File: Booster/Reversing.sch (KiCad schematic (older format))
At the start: 13 parts

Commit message: Getting close to feature complete for a single channel.
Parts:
- removed R?: R, symbol R
- added P?: REVERSER_OUT_OP, symbol CONN_01X02
- added R?: R, symbol R
- added U?: PC817, Housings_DIP:DIP-4_W7.62mm, symbol PC817
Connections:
- wire segments 33 -> 49
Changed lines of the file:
@@
 	0    1    1    0
 $EndComp
-Wire Wire Line
-	3050 4400 4250 4400
-Wire Wire Line
-	4250 4600 3050 4600
 $Comp
 L +5V #PWR?
@@
 	-1   0    0    1
 $EndComp
-Wire Wire Line
-	2750 4400 2600 4400
-Wire Wire Line
-	2600 4400 2600 4950
-Wire Wire Line
-	2750 4600 2600 4600
-Connection ~ 2600 4600
 Text Label 3500 4600 0    60   ~ 0
 IR_Led
@@
 	1    0    0    -1
 $EndComp
-Wire Wire Line
-	4100 4100 4100 4200
-Wire Wire Line
-	4100 4200 4250 4200
 $Comp
 L LM339 U?
@@
 	1    0    0    -1
 $EndComp
-Wire Wire Line
-	4050 3450 4800 3450
-Wire Wire Line
-	4300 3450 4300 3300
-Wire Wire Line
-	4600 3450 4600 2700
-Wire Wire Line
-	4600 2700 4850 2700
-Connection ~ 4300 3450
 $Comp
 L +5V #PWR?
@@
 	1    0    0    -1
 $EndComp
-Wire Wire Line
-	4300 2900 4300 3000
-Wire Wire Line
-	3150 4400 3150 3550
-Wire Wire Line
-	3150 3550 3450 3550
-Connection ~ 3150 4400
 $Comp
 L POT_TRIM RV?
@@
 	1    0    0    -1
 $EndComp
-Wire Wire Line
-	2950 3350 3450 3350
-Wire Wire Line
-	2800 3500 2800 3700
-Wire Wire Line
-	2800 2900 2800 3200
 $Comp
 L +5V #PWR?
@@
 	1    0    0    -1
 $EndComp
-Wire Wire Line
-	2350 2500 4850 2500
-Wire Wire Line
-	7250 2600 6050 2600
 $Comp
 L BC807-40 Q?
@@
 	0    1    1    0
 $EndComp
-Connection ~ 4600 3450
-Wire Wire Line
-	5100 3450 5300 3450
 $Comp
 L LED D?
@@
 	0    1    1    0
 $EndComp
-Wire Wire Line
-	5600 3250 5600 3150
-Wire Wire Line
-	5600 3150 6450 3150
-Wire Wire Line
-	6750 3150 7000 3150
-Wire Wire Line
-	7300 3150 7400 3150
-Wire Wire Line
-	7400 3150 7400 3800
-Wire Wire Line
-	5600 3650 5600 4050
-Wire Wire Line
-	5600 4050 5350 4050
-Wire Wire Line
-	5350 4050 5350 3900
 $Comp
 L +5V #PWR?
@@
 $EndComp
 Wire Wire Line
+	3050 4400 3150 4400
+Wire Wire Line
+	3150 4400 4250 4400
+Wire Wire Line
+	4250 4600 3050 4600
+Wire Wire Line
+	2750 4400 2600 4400
+Wire Wire Line
+	2600 4400 2600 4600
+Wire Wire Line
+	2600 4600 2600 4950
+Wire Wire Line
+	2750 4600 2600 4600
+Connection ~ 2600 4600
+Wire Wire Line
+	4100 4100 4100 4200
+Wire Wire Line
+	4100 4200 4250 4200
+Wire Wire Line
+	4050 3450 4300 3450
+Wire Wire Line
+	4300 3450 4600 3450
+Wire Wire Line
+	4600 3450 4800 3450
+Wire Wire Line
+	4300 3450 4300 3300
+Wire Wire Line
+	4600 2700 4600 3450
+Wire Wire Line
+	4600 3450 4600 3800
+Wire Wire Line
+	4600 2700 4850 2700
+Connection ~ 4300 3450
+Wire Wire Line
+	4300 2900 4300 3000
+Wire Wire Line
+	3150 4400 3150 3550
+Wire Wire Line
+	3150 3550 3450 3550
+Connection ~ 3150 4400
+Wire Wire Line
+	2950 3350 3450 3350
+Wire Wire Line
+	2800 3500 2800 3700
+Wire Wire Line
+	2800 2900 2800 3200
+Wire Wire Line
+	2350 2500 4850 2500
+Wire Wire Line
+	7250 2600 6050 2600
+Connection ~ 4600 3450
+Wire Wire Line
+	5100 3450 5300 3450
+Wire Wire Line
+	5600 3250 5600 3150
+Wire Wire Line
+	5600 3150 6350 3150
+Wire Wire Line
+	6350 3150 6450 3150
+Wire Wire Line
+	6750 3150 7000 3150
+Wire Wire Line
+	7300 3150 7400 3150
+Wire Wire Line
+	7400 3150 7400 3800
+Wire Wire Line
+	5600 3650 5600 4050
+Wire Wire Line
+	5600 4050 5350 4050
+Wire Wire Line
+	5350 4050 5350 3900
+Wire Wire Line
 	6350 3150 6350 3750
+Wire Wire Line
+	6350 3750 6350 4400
 Wire Wire Line
 	6350 3750 6500 3750
 Connection ~ 6350 3150
+Wire Wire Line
+	6500 3850 6450 3850
+Wire Wire Line
+	6450 3850 6450 4100
+$Comp
+L GND #PWR?
+U 1 1 5A0EF583
+P 6450 4100
+F 0 "#PWR?" H 6450 3850 50  0001 C CNN
+F 1 "GND" H 6450 3950 50  0000 C CNN
+F 2 "" H 6450 4100 50  0001 C CNN
+F 3 "" H 6450 4100 50  0001 C CNN
+	1    6450 4100
+	1    0    0    -1
+$EndComp
+Connection ~ 6350 3750
 $Comp
 L R R?
-U 1 1 5A08AD53
-P 6200 3500
-F 0 "R?" V 6280 3500 50  0000 C CNN
-F 1 "R" V 6200 3500 50  0000 C CNN
-F 2 "" V 6130 3500 50  0000 C CNN
-F 3 "" H 6200 3500 50  0000 C CNN
-	1    6200 3500
-	1    0    0    -1
-$EndComp
-Wire Wire Line
-	6200 3350 6200 3150
-Connection ~ 6200 3150
-Wire Wire Line
-	6200 3650 6200 4100
-Wire Wire Line
-	6500 3850 6200 3850
-Connection ~ 6200 3850
-$Comp
-L GND #PWR?
-U 1 1 5A08AE8D
-P 6200 4100
-F 0 "#PWR?" H 6200 3850 50  0001 C CNN
-F 1 "GND" H 6200 3950 50  0000 C CNN
-F 2 "" H 6200 4100 50  0000 C CNN
-F 3 "" H 6200 4100 50  0000 C CNN
-	1    6200 4100
-	1    0    0    -1
-$EndComp
+U 1 1 5A0EF5E4
+P 6350 4550
+F 0 "R?" V 6430 4550 50  0000 C CNN
+F 1 "R" V 6350 4550 50  0000 C CNN
+F 2 "" V 6280 4550 50  0001 C CNN
+F 3 "" H 6350 4550 50  0001 C CNN
+	1    6350 4550
+	1    0    0    -1
+$EndComp
+Wire Wire Line
+	6350 4700 6350 4800
+Wire Wire Line
+	6350 4800 6550 4800
+$Comp
+L PC817 U?
+U 1 1 5A0EF66A
+P 6850 4900
+F 0 "U?" H 6650 5100 50  0000 L CNN
+F 1 "PC817" H 6850 5100 50  0000 L CNN
+F 2 "Housings_DIP:DIP-4_W7.62mm" H 6650 4700 50  0001 L CIN
+F 3 "" H 6850 4900 50  0001 L CNN
+	1    6850 4900
+	1    0    0    -1
+$EndComp
+$Comp
+L CONN_01X02 P?
+U 1 1 5A0EF6BB
+P 7650 4900
+F 0 "P?" H 7650 5050 50  0000 C CNN
+F 1 "REVERSER_OUT_OP" V 7750 4900 50  0000 C CNN
+F 2 "" H 7650 4900 50  0000 C CNN
+F 3 "" H 7650 4900 50  0000 C CNN
+	1    7650 4900
+	1    0    0    -1
+$EndComp
+Wire Wire Line
+	7450 4850 7350 4850
+Wire Wire Line
+	7350 4850 7350 4800
+Wire Wire Line
+	7350 4800 7150 4800
+Wire Wire Line
+	7150 5000 7350 5000
+Wire Wire Line
+	7350 5000 7350 4950
+Wire Wire Line
+	7350 4950 7450 4950
+$Comp
+L GND #PWR?
+U 1 1 5A0EF7FA
+P 6350 5200
+F 0 "#PWR?" H 6350 4950 50  0001 C CNN
+F 1 "GND" H 6350 5050 50  0000 C CNN
+F 2 "" H 6350 5200 50  0001 C CNN
+F 3 "" H 6350 5200 50  0001 C CNN
+	1    6350 5200
+	1    0    0    -1
+$EndComp
+Wire Wire Line
+	6350 5200 6350 5000
+Wire Wire Line
+	6350 5000 6550 5000
 $EndSCHEMATC

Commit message: Added meassurement tabs and other general "finalizing touches"
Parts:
- removed J?: Screw_Terminal_1x03, symbol Screw_Terminal_1x03
- added J? (x2): Conn_01x01, symbol Conn_01x01
- added J?: Conn_01x04, symbol Conn_01x04
- added R?: 10K, symbol R
- added R?: ?100, symbol R
- added SW?: SW_SPST_x02, symbol SW_SPST_x02
- added U?: 74HC86, symbol 74LS86
- R?: value 100 -> 220
- R?: value R -> 10K
- U?: value 74LS86 -> 74HC86
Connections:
- net labels added: Indicator_LED
- wire segments 49 -> 59
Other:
- note added: "Invert detector\nFor IR reflective/direct support."
- moved on the sheet: R?, RV?, U?A

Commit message: Reference voltage of reverser is now the 1V after the resistor dropper. This allows running one wire less to the sensor unit, at the cost of the photo resistor only working off 1V.
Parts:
- removed SW?: SW_SPST_x02, symbol SW_SPST_x02
- added SW?: SW_SPST_x03, symbol SW_SPST_x03
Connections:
- wire segments 59 -> 63
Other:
- moved on the sheet: R?
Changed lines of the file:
@@
 L R R?
 U 1 1 5A089B6E
-P 1250 4300
-F 0 "R?" V 1330 4300 50  0000 C CNN
-F 1 "10K" V 1250 4300 50  0000 C CNN
-F 2 "" V 1180 4300 50  0000 C CNN
-F 3 "" H 1250 4300 50  0000 C CNN
-	1    1250 4300
+P 1050 4300
+F 0 "R?" V 1130 4300 50  0000 C CNN
+F 1 "10K" V 1050 4300 50  0000 C CNN
+F 2 "" V 980 4300 50  0000 C CNN
+F 3 "" H 1050 4300 50  0000 C CNN
+	1    1050 4300
 	0    1    1    0
 $EndComp
@@
 F 3 "" H 1150 3250 50  0000 C CNN
 	1    1150 3250
-	1    0    0    -1
-$EndComp
-$Comp
-L +5V #PWR?
-U 1 1 5A08A48D
-P 1150 2800
-F 0 "#PWR?" H 1150 2650 50  0001 C CNN
-F 1 "+5V" H 1150 2940 50  0000 C CNN
-F 2 "" H 1150 2800 50  0000 C CNN
-F 3 "" H 1150 2800 50  0000 C CNN
-	1    1150 2800
-	1    0    0    -1
-$EndComp
-$Comp
-L GND #PWR?
-U 1 1 5A08A4CA
-P 1150 3600
-F 0 "#PWR?" H 1150 3350 50  0001 C CNN
-F 1 "GND" H 1150 3450 50  0000 C CNN
-F 2 "" H 1150 3600 50  0000 C CNN
-F 3 "" H 1150 3600 50  0000 C CNN
-	1    1150 3600
 	1    0    0    -1
 $EndComp
@@
 $EndComp
 $Comp
-L SW_SPST_x02 SW?
-U 2 1 5A0F584C
-P 3350 4250
-F 0 "SW?" H 3350 4375 50  0000 C CNN
-F 1 "SW_SPST_x02" H 3350 4150 50  0000 C CNN
-F 2 "" H 3350 4250 50  0001 C CNN
-F 3 "" H 3350 4250 50  0001 C CNN
-	2    3350 4250
-	0    1    1    0
-$EndComp
-$Comp
 L +5V #PWR?
 U 1 1 5A0F5A28
@@
 L R R?
 U 1 1 5A089977
-P 1250 4500
-F 0 "R?" V 1330 4500 50  0000 C CNN
-F 1 "220" V 1250 4500 50  0000 C CNN
-F 2 "" V 1180 4500 50  0000 C CNN
-F 3 "" H 1250 4500 50  0000 C CNN
-	1    1250 4500
+P 1050 4500
+F 0 "R?" V 1130 4500 50  0000 C CNN
+F 1 "220" V 1050 4500 50  0000 C CNN
+F 2 "" V 980 4500 50  0000 C CNN
+F 3 "" H 1050 4500 50  0000 C CNN
+	1    1050 4500
 	0    1    1    0
 $EndComp
@@
 $EndComp
 Wire Wire Line
-	2200 4500 1400 4500
+	2200 4500 1200 4500
 Wire Wire Line
 	2200 4500 2200 4400
 Wire Wire Line
-	1400 4300 2500 4300
+	1200 4300 2500 4300
 Wire Wire Line
 	2200 4400 2500 4400
 Connection ~ 6350 4300
 Wire Wire Line
-	5800 4300 6350 4300
-Wire Wire Line
-	5800 5100 5800 4300
-Wire Wire Line
-	3400 5100 5800 5100
+	6350 4300 5800 4300
+Wire Wire Line
+	5800 4300 5800 5100
+Wire Wire Line
+	5800 5100 3400 5100
 Wire Wire Line
 	2300 5100 3100 5100
@@
 	2350 2500 4850 2500
 Wire Wire Line
-	1150 2800 1150 3100
-Wire Wire Line
-	1150 3400 1150 3600
-Wire Wire Line
 	1300 3250 1800 3250
 Connection ~ 1500 4300
@@
 	2400 3350 3450 3350
 Wire Wire Line
-	950  4500 1100 4500
-Wire Wire Line
-	1100 4300 950  4300
+	750  4500 900  4500
+Wire Wire Line
+	900  4300 750  4300
 Wire Wire Line
 	2500 4600 2400 4600
@@
 L +5V #PWR?
 U 1 1 5A104760
-P 950 4150
-F 0 "#PWR?" H 950 4000 50  0001 C CNN
-F 1 "+5V" H 950 4290 50  0000 C CNN
-F 2 "" H 950 4150 50  0001 C CNN
-F 3 "" H 950 4150 50  0001 C CNN
-	1    950  4150
-	1    0    0    -1
-$EndComp
-Connection ~ 950  4300
-Wire Wire Line
-	950  4150 950  4500
+P 750 4150
+F 0 "#PWR?" H 750 4000 50  0001 C CNN
+F 1 "+5V" H 750 4290 50  0000 C CNN
+F 2 "" H 750 4150 50  0001 C CNN
+F 3 "" H 750 4150 50  0001 C CNN
+	1    750  4150
+	1    0    0    -1
+$EndComp
+Connection ~ 750  4300
+Wire Wire Line
+	750  4150 750  4500
+$Comp
+L SW_SPST_x03 SW?
+U 3 1 5A1068DB
+P 3350 4250
+F 0 "SW?" H 3350 4375 50  0000 C CNN
+F 1 "SW_SPST_x03" H 3350 4150 50  0000 C CNN
+F 2 "" H 3350 4250 50  0001 C CNN
+F 3 "" H 3350 4250 50  0001 C CNN
+	3    3350 4250
+	0    1    1    0
+$EndComp
+Wire Wire Line
+	1150 3400 1150 3750
+Wire Wire Line
+	1150 3750 1350 3750
+Wire Wire Line
+	1350 3750 1350 4500
+Connection ~ 1350 4500
+Wire Wire Line
+	1150 3100 1150 2800
+Wire Wire Line
+	1150 2800 750  2800
+Wire Wire Line
+	750  2800 750  3100
+$Comp
+L GND #PWR?
+U 1 1 5A114B43
+P 750 3100
+F 0 "#PWR?" H 750 2850 50  0001 C CNN
+F 1 "GND" H 750 2950 50  0000 C CNN
+F 2 "" H 750 3100 50  0001 C CNN
+F 3 "" H 750 3100 50  0001 C CNN
+	1    750  3100
+	1    0    0    -1
+$EndComp
 $EndSCHEMATC

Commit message: Use actual test point instead of 1 pin jumpers.
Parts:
- removed J? (x2): Conn_01x01, symbol Conn_01x01
- added TP? (x2): TEST, symbol TEST
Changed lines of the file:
@@
 $Comp
 L 74LS86 U?
-U 1 1 5A0898F2
+U 4 1 5A0898F2
 P 5450 2600
 F 0 "U?" H 5500 2650 50  0000 C CNN
@@
 F 2 "" H 5450 2600 50  0000 C CNN
 F 3 "" H 5450 2600 50  0000 C CNN
-	1    5450 2600
+	4    5450 2600
 	1    0    0    -1
 $EndComp
@@
 Invert detector\nFor IR reflective/direct support.
 $Comp
-L Conn_01x01 J?
-U 1 1 5A0F9C51
-P 1700 3650
-F 0 "J?" H 1700 3750 50  0000 C CNN
-F 1 "Conn_01x01" H 1700 3550 50  0000 C CNN
-F 2 "" H 1700 3650 50  0001 C CNN
-F 3 "" H 1700 3650 50  0001 C CNN
-	1    1700 3650
-	0    1    1    0
-$EndComp
-$Comp
-L Conn_01x01 J?
-U 1 1 5A0F9CB3
-P 1500 3050
-F 0 "J?" H 1500 3150 50  0000 C CNN
-F 1 "Conn_01x01" H 1500 2950 50  0000 C CNN
-F 2 "" H 1500 3050 50  0001 C CNN
-F 3 "" H 1500 3050 50  0001 C CNN
-	1    1500 3050
-	0    -1   -1   0
-$EndComp
-$Comp
 L R R?
 U 1 1 5A089977
@@
 	1    0    0    -1
 $EndComp
+$Comp
+L TEST TP?
+U 1 1 5A164BED
+P 1650 3250
+F 0 "TP?" H 1650 3550 50  0000 C BNN
+F 1 "TEST" H 1650 3500 50  0000 C CNN
+F 2 "" H 1650 3250 50  0001 C CNN
+F 3 "" H 1650 3250 50  0001 C CNN
+	1    1650 3250
+	1    0    0    -1
+$EndComp
+$Comp
+L TEST TP?
+U 1 1 5A164C44
+P 1650 3450
+F 0 "TP?" H 1650 3750 50  0000 C BNN
+F 1 "TEST" H 1650 3700 50  0000 C CNN
+F 2 "" H 1650 3450 50  0001 C CNN
+F 3 "" H 1650 3450 50  0001 C CNN
+	1    1650 3450
+	-1   0    0    1
+$EndComp
 $EndSCHEMATC

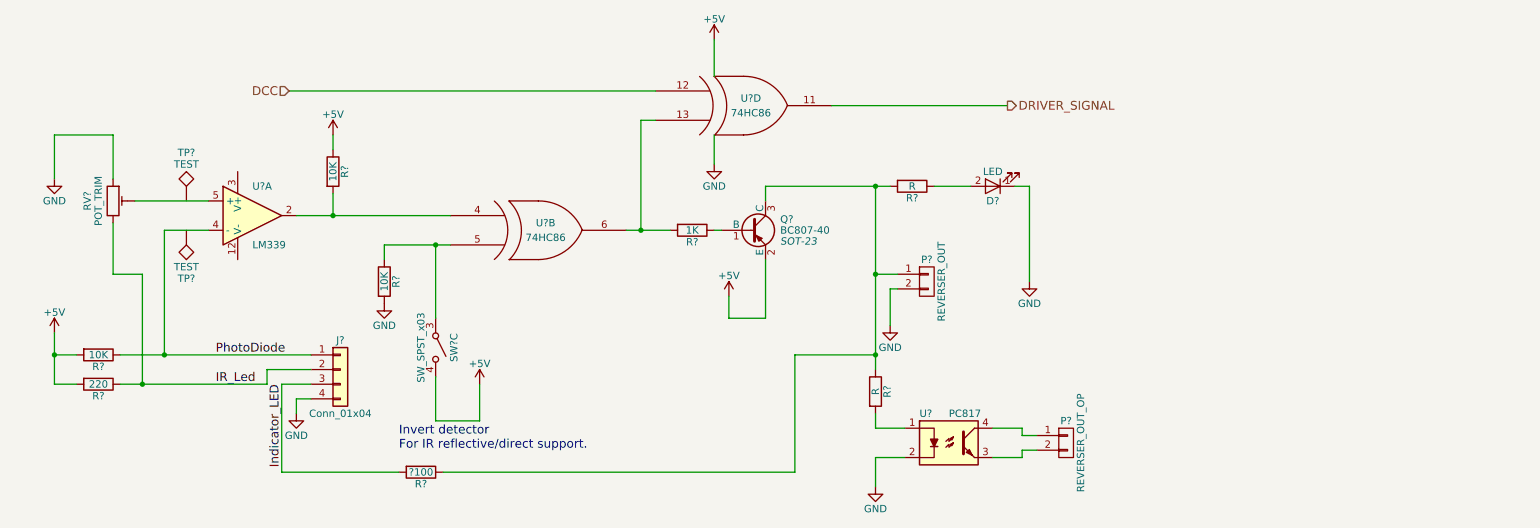
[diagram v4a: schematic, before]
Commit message: Minor fixes based on breadboard experiments.
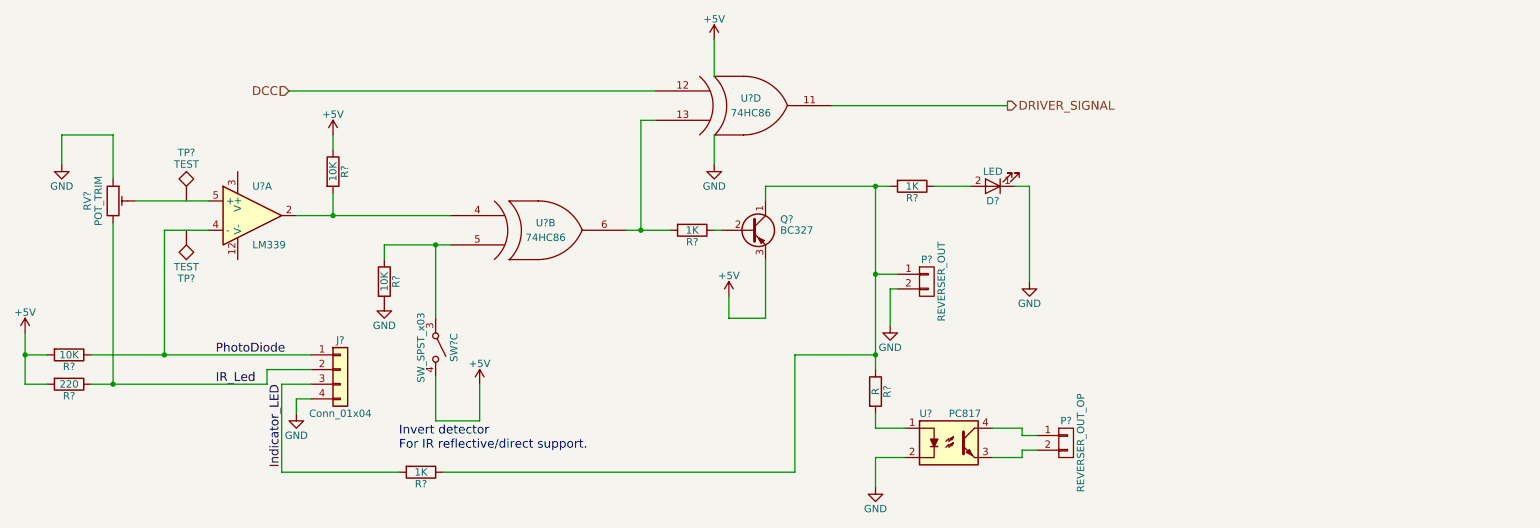
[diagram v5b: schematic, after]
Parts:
- removed Q?: BC807-40, SOT-23, symbol BC807-40
- added Q?: BC327, TO_SOT_Packages_THT:TO-92_Molded_Narrow, symbol BC327
- R?: value R -> 1K
- R?: value ?100 -> 1K
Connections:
- net +5V: now also Q?.3 (E)
- net at R?.1: now also Q?.2 (B)
- net at P?.1 (P1), R?.1, R?.1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: now also Q?.1 (C)
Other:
- moved on the sheet: R?
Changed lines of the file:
@@
 L R R?
 U 1 1 5A089B6E
-P 1050 4300
-F 0 "R?" V 1130 4300 50  0000 C CNN
-F 1 "10K" V 1050 4300 50  0000 C CNN
-F 2 "" V 980 4300 50  0000 C CNN
-F 3 "" H 1050 4300 50  0000 C CNN
-	1    1050 4300
+P 850 4300
+F 0 "R?" V 930 4300 50  0000 C CNN
+F 1 "10K" V 850 4300 50  0000 C CNN
+F 2 "" V 780 4300 50  0000 C CNN
+F 3 "" H 850 4300 50  0000 C CNN
+	1    850  4300
 	0    1    1    0
 $EndComp
@@
 F 3 "" H 1150 3250 50  0000 C CNN
 	1    1150 3250
-	1    0    0    -1
-$EndComp
-$Comp
-L BC807-40 Q?
-U 1 1 5A08A72D
-P 5500 3450
-F 0 "Q?" H 5700 3525 50  0000 L CNN
-F 1 "BC807-40" H 5700 3450 50  0000 L CNN
-F 2 "SOT-23" H 5700 3375 50  0000 L CIN
-F 3 "" H 5500 3450 50  0000 L CNN
-	1    5500 3450
 	1    0    0    -1
 $EndComp
@@
 P 6600 3150
 F 0 "R?" V 6680 3150 50  0000 C CNN
-F 1 "R" V 6600 3150 50  0000 C CNN
+F 1 "1K" V 6600 3150 50  0000 C CNN
 F 2 "" V 6530 3150 50  0000 C CNN
 F 3 "" H 6600 3150 50  0000 C CNN
@@
 L R R?
 U 1 1 5A089977
-P 1050 4500
-F 0 "R?" V 1130 4500 50  0000 C CNN
-F 1 "220" V 1050 4500 50  0000 C CNN
-F 2 "" V 980 4500 50  0000 C CNN
-F 3 "" H 1050 4500 50  0000 C CNN
-	1    1050 4500
+P 850 4500
+F 0 "R?" V 930 4500 50  0000 C CNN
+F 1 "220" V 850 4500 50  0000 C CNN
+F 2 "" V 780 4500 50  0000 C CNN
+F 3 "" H 850 4500 50  0000 C CNN
+	1    850  4500
 	0    1    1    0
 $EndComp
@@
 P 3250 5100
 F 0 "R?" V 3330 5100 50  0000 C CNN
-F 1 "?100" V 3250 5100 50  0000 C CNN
+F 1 "1K" V 3250 5100 50  0000 C CNN
 F 2 "" V 3180 5100 50  0001 C CNN
 F 3 "" H 3250 5100 50  0001 C CNN
@@
 $EndComp
 Wire Wire Line
-	2200 4500 1200 4500
+	2200 4500 1000 4500
 Wire Wire Line
 	2200 4500 2200 4400
 Wire Wire Line
-	1200 4300 2500 4300
+	1000 4300 2500 4300
 Wire Wire Line
 	2200 4400 2500 4400
@@
 	2400 3350 3450 3350
 Wire Wire Line
-	750  4500 900  4500
-Wire Wire Line
-	900  4300 750  4300
+	550  4500 700  4500
+Wire Wire Line
+	700  4300 550  4300
 Wire Wire Line
 	2500 4600 2400 4600
@@
 L +5V #PWR?
 U 1 1 5A104760
-P 750 4150
-F 0 "#PWR?" H 750 4000 50  0001 C CNN
-F 1 "+5V" H 750 4290 50  0000 C CNN
-F 2 "" H 750 4150 50  0001 C CNN
-F 3 "" H 750 4150 50  0001 C CNN
-	1    750  4150
-	1    0    0    -1
-$EndComp
-Connection ~ 750  4300
-Wire Wire Line
-	750  4150 750  4500
+P 550 4150
+F 0 "#PWR?" H 550 4000 50  0001 C CNN
+F 1 "+5V" H 550 4290 50  0000 C CNN
+F 2 "" H 550 4150 50  0001 C CNN
+F 3 "" H 550 4150 50  0001 C CNN
+	1    550  4150
+	1    0    0    -1
+$EndComp
+Connection ~ 550  4300
+Wire Wire Line
+	550  4150 550  4500
 $Comp
 L SW_SPST_x03 SW?
@@
 $EndComp
 Wire Wire Line
-	1150 3400 1150 3750
-Wire Wire Line
-	1150 3750 1350 3750
-Wire Wire Line
-	1350 3750 1350 4500
-Connection ~ 1350 4500
+	1150 3400 1150 4500
 Wire Wire Line
 	1150 3100 1150 2800
-Wire Wire Line
-	1150 2800 750  2800
-Wire Wire Line
-	750  2800 750  3100
-$Comp
-L GND #PWR?
-U 1 1 5A114B43
-P 750 3100
-F 0 "#PWR?" H 750 2850 50  0001 C CNN
-F 1 "GND" H 750 2950 50  0000 C CNN
-F 2 "" H 750 3100 50  0001 C CNN
-F 3 "" H 750 3100 50  0001 C CNN
-	1    750  3100
-	1    0    0    -1
-$EndComp
 $Comp
 L TEST TP?
@@
 	-1   0    0    1
 $EndComp
+Connection ~ 1150 4500
+Wire Wire Line
+	1150 2800 800  2800
+Wire Wire Line
+	800  2800 800  3000
+$Comp
+L GND #PWR?
+U 1 1 5A19FF1E
+P 800 3000
+F 0 "#PWR?" H 800 2750 50  0001 C CNN
+F 1 "GND" H 800 2850 50  0000 C CNN
+F 2 "" H 800 3000 50  0000 C CNN
+F 3 "" H 800 3000 50  0000 C CNN
+	1    800  3000
+	1    0    0    -1
+$EndComp
+$Comp
+L BC327 Q?
+U 1 1 5A1A0226
+P 5500 3450
+F 0 "Q?" H 5700 3525 50  0000 L CNN
+F 1 "BC327" H 5700 3450 50  0000 L CNN
+F 2 "TO_SOT_Packages_THT:TO-92_Molded_Narrow" H 5700 3375 50  0001 L CIN
+F 3 "" H 5500 3450 50  0001 L CNN
+	1    5500 3450
+	1    0    0    -1
+$EndComp
 $EndSCHEMATC
